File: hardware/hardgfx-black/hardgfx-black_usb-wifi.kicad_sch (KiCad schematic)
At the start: 29 parts, among them J22 USB_OTG, J23 WIFI_GPIO, J24 WIFI_GPIO, J25 Boot option, J26 WIFI_UART, J27 JTAG, Q1 BSR14, SW2 SW_MEC_5E, SW3 WIFI_UART, U10 USBLC6-4SC6, U11 ESP32-WROOM-32, U9 STMPS2151MTR

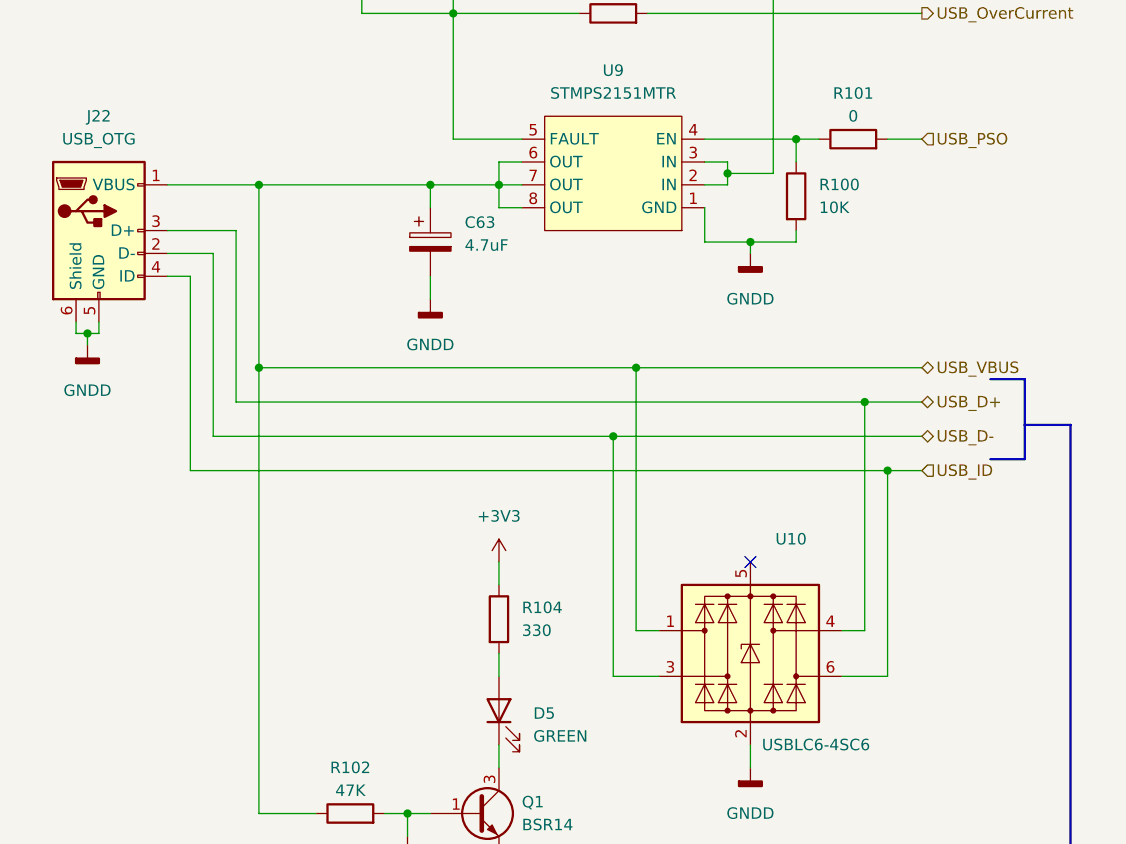
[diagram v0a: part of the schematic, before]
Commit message: Finish first schematic version.
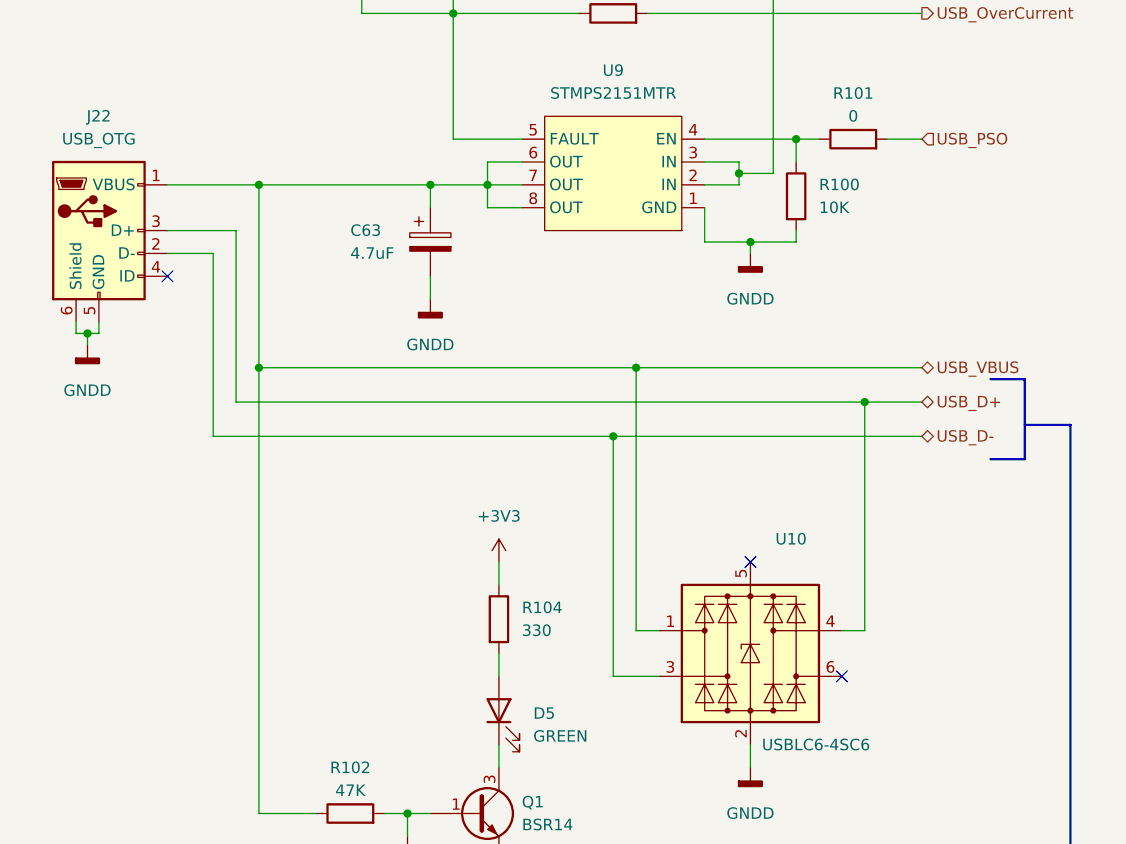
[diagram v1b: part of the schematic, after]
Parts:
- J23, J24: MANUFACTURER Molex -> Samtec Inc.; digikey# 0702800593-ND -> SAM1029-10-ND; manf# 0702800593 -> TSW-110-07-G-S; mouser# 538-70280-0593 -> 200-TSW11007GS
- J25, J26: MANUFACTURER Molex -> Samtec Inc.; digikey# 0423752486-ND -> SAM1029-02-ND; manf# 0423752486 -> TSW-102-07-G-S; mouser# 538-42375-2486 -> 200-TSW10207GS
- J27: footprint Connector_PinHeader_2.54mm:PinHeader_1x04_P2.54mm_Vertical -> Connector_PinSocket_2.54mm:PinSocket_1x04_P2.54mm_Vertical; MANUFACTURER Molex -> Samtec Inc.; digikey# 0423752523-ND -> SAM1029-04-ND; manf# 0423752523 -> TSW-104-07-G-S; mouser# 538-42375-2523 -> 200-TSW10407GS
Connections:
- net USB_ID: no longer names the net of U10.6 (I/O4)
- net USB_ID: no longer J22.4 (ID)
- no-connect marks 7 -> 9

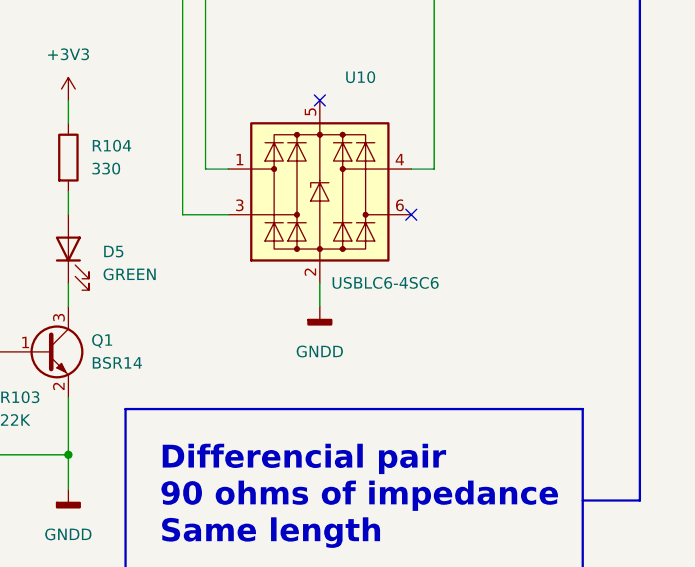
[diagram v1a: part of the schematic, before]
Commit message: Adding application note PDF document and change backlight controller.
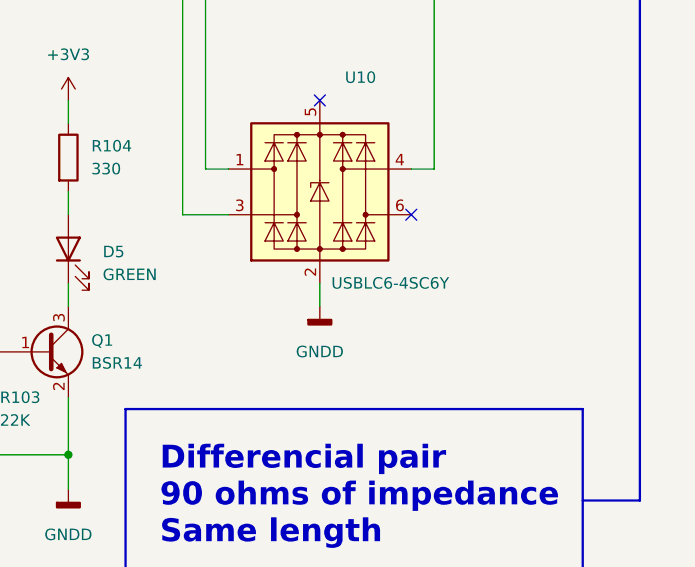
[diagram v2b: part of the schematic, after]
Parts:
- U10: value USBLC6-4SC6 -> USBLC6-4SC6Y; footprint Package_TO_SOT_SMD:SOT-23-6 -> Package_TO_SOT_SMD:SOT-23-6_Handsoldering; digikey# 497-4492-1-ND -> 497-11883-1-ND; manf# USBLC6-4SC6 -> USBLC6-4SC6Y; mouser# 511-USBLC6-4SC6 -> 511-USBLC6-4SC6Y
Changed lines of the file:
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@@
       (effects (font (size 1.27 1.27)) (justify left))
     )
-    (property "Value" "USBLC6-4SC6" (id 1) (at 246.38 129.54 0)
+    (property "Value" "USBLC6-4SC6Y" (id 1) (at 246.38 129.54 0)
       (effects (font (size 1.27 1.27)) (justify left))
     )
-    (property "Footprint" "Package_TO_SOT_SMD:SOT-23-6" (id 2) (at 245.11 132.08 0)
+    (property "Footprint" "Package_TO_SOT_SMD:SOT-23-6_Handsoldering" (id 2) (at 245.11 132.08 0)
       (effects (font (size 1.27 1.27)) hide)
     )
-    (property "Datasheet" "https://www.st.com/resource/en/datasheet/usblc6-4.pdf" (id 3) (at 250.19 110.49 0)
+    (property "Datasheet" "https://www.st.com/content/ccc/resource/technical/document/datasheet/4d/3b/c6/28/1e/a5/40/1d/DM00055251.pdf/files/DM00055251.pdf/jcr:content/translations/en.DM00055251.pdf" (id 3) (at 250.19 110.49 0)
       (effects (font (size 1.27 1.27)) hide)
     )
@@
       (effects (font (size 1.27 1.27)) hide)
     )
-    (property "manf#" "USBLC6-4SC6" (id 5) (at 245.11 119.38 0)
+    (property "manf#" "USBLC6-4SC6Y" (id 5) (at 245.11 119.38 0)
       (effects (font (size 1.27 1.27)) hide)
     )
-    (property "digikey#" "497-4492-1-ND" (id 6) (at 245.11 119.38 0)
+    (property "digikey#" "497-11883-1-ND" (id 6) (at 245.11 119.38 0)
       (effects (font (size 1.27 1.27)) hide)
     )
-    (property "mouser#" "511-USBLC6-4SC6" (id 7) (at 245.11 119.38 0)
+    (property "mouser#" "511-USBLC6-4SC6Y" (id 7) (at 245.11 119.38 0)
       (effects (font (size 1.27 1.27)) hide)
     )
